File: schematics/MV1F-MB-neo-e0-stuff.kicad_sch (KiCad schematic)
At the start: 5 parts

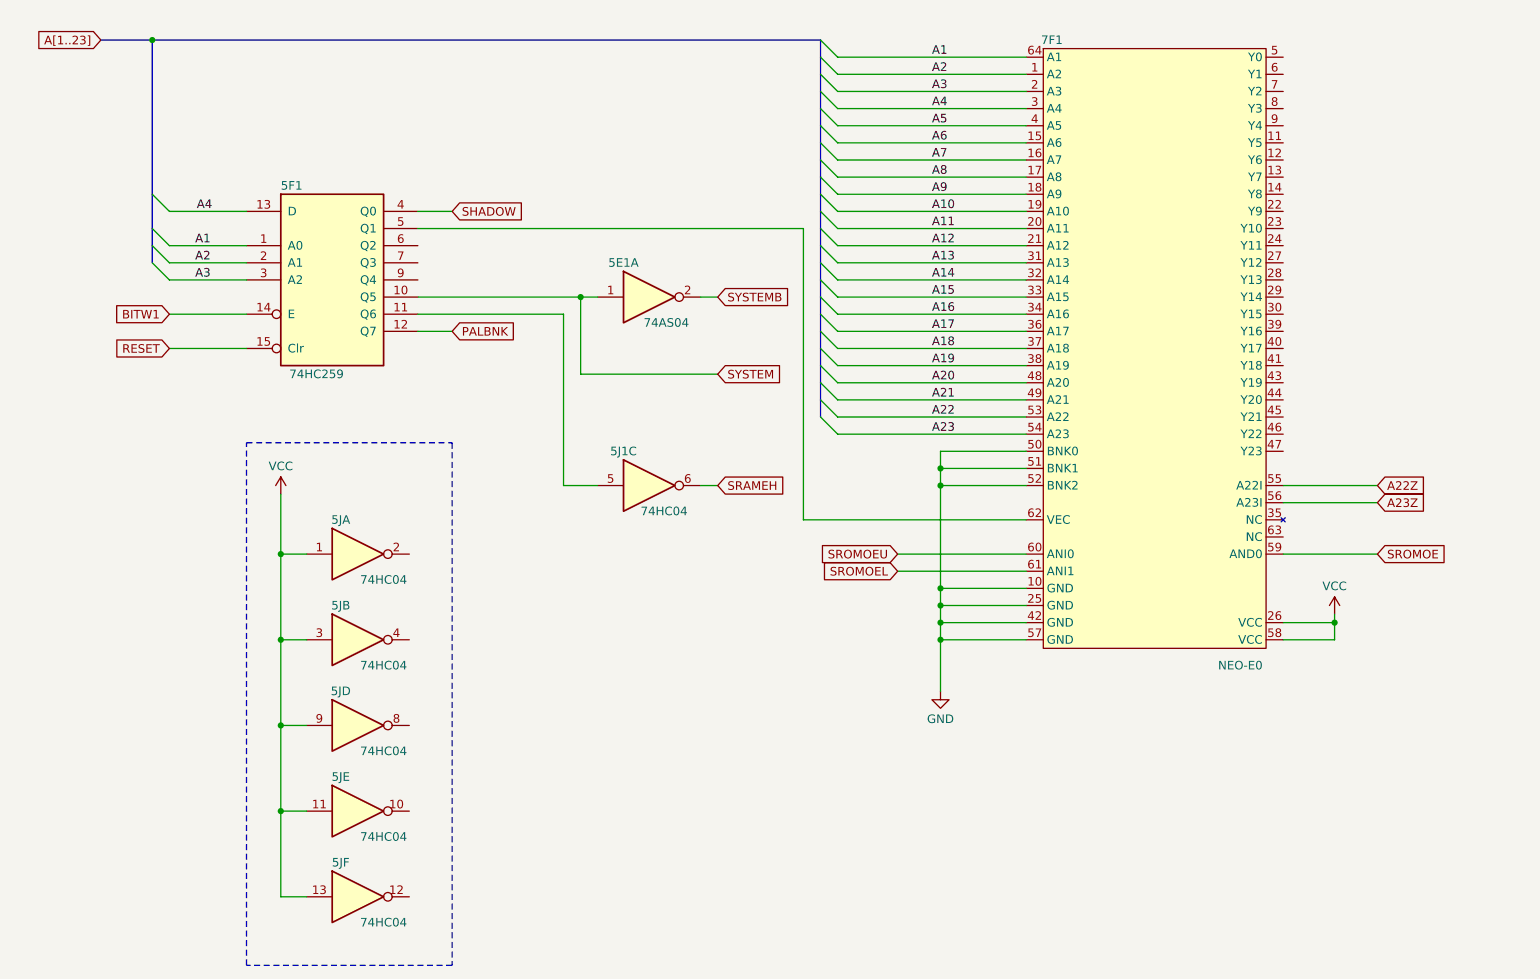
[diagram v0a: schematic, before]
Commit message: Typo... and orphan labels remove
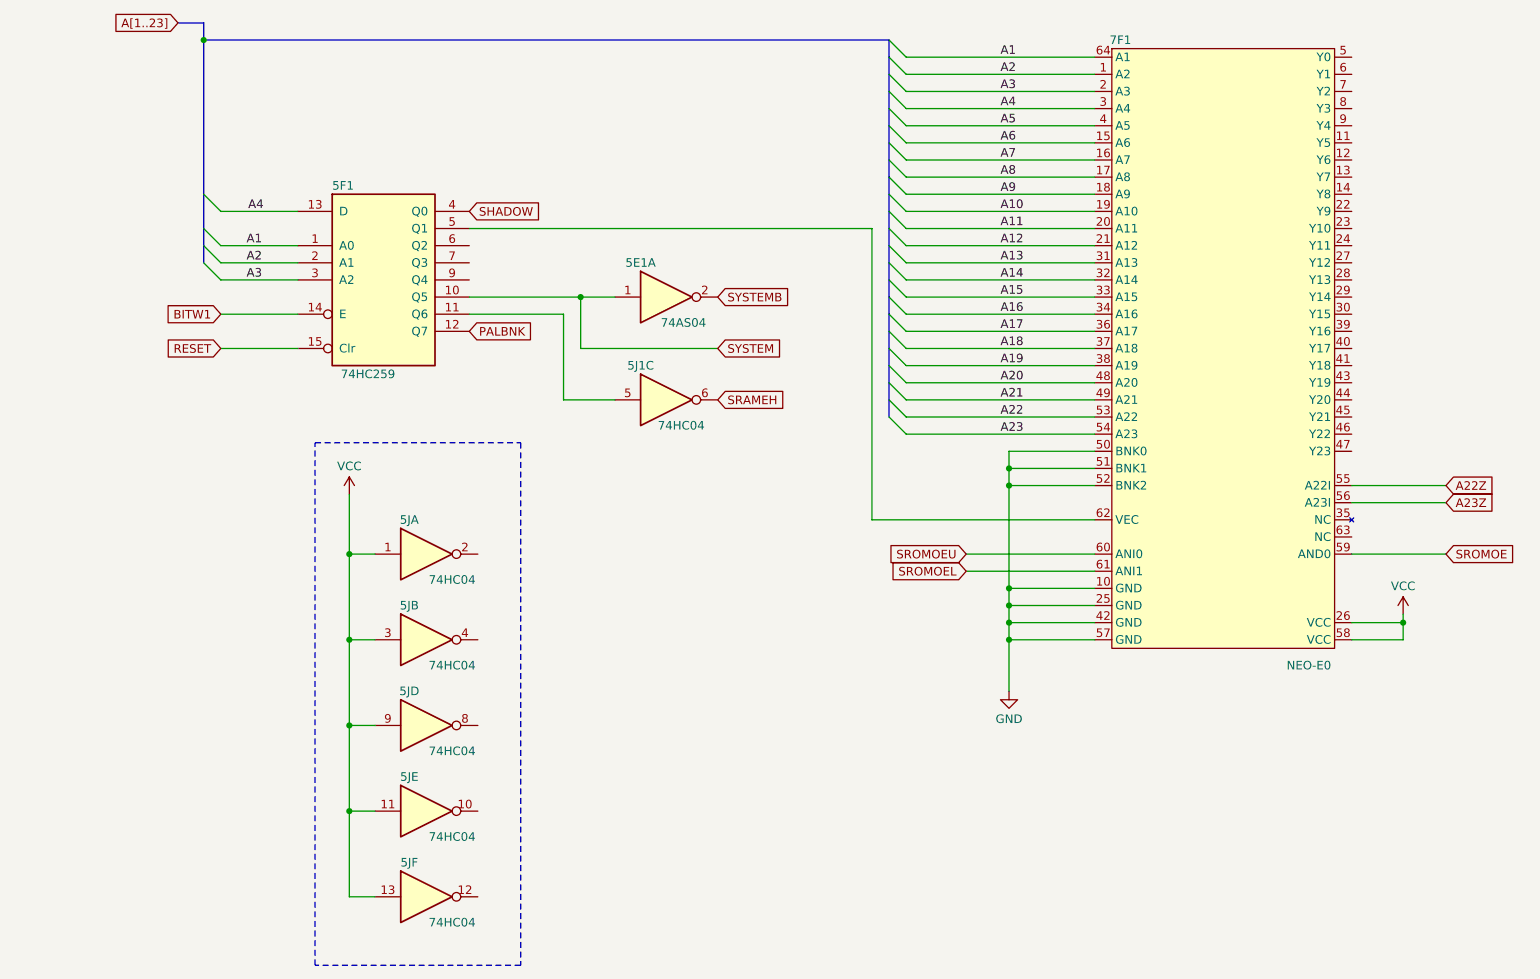
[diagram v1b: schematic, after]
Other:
- moved on the sheet: 5E1A, 5F1, 5J1C, 5JA, 5JB, 5JD, 5JE, 5JF, 7F1

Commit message: Typo
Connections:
- net SRAMEH renamed BRAMEN
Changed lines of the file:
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@@
     )
   )
-  (global_label "SRAMEH" (shape input) (at 121.92 71.12 0) (fields_autoplaced)
+  (global_label "BRAMEN" (shape input) (at 121.92 71.12 0) (fields_autoplaced)
     (effects (font (size 1.27 1.27)) (justify left))
-    (property "Intersheetrefs" "${INTERSHEET_REFS}" (at 132.4042 71.12 0)
+    (property "Intersheetrefs" "${INTERSHEET_REFS}" (at 132.4647 71.12 0)
       (effects (font (size 1.27 1.27)) (justify left))
     )
